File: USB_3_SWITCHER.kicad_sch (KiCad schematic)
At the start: 0 parts

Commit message: Arbeit
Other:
- sheet UPSTREAM_CON ports: added USB_UP_D_N, USB_UP_D_P, USB_UP_PORT_POWER_ON, USB_UP_SSRX_C_N, USB_UP_SSRX_C_P, USB_UP_SSTX_C_N, USB_UP_SSTX_C_P; removed none
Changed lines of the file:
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@@
 	)
 	(sheet
-		(at 135.89 133.35)
+		(at 134.62 133.35)
 		(size 41.91 59.69)
 		(exclude_from_sim no)
@@
 		)
 		(property "Sheetname" "HS_MUX"
-			(at 135.89 132.6384 0)
+			(at 134.62 132.6384 0)
 			(effects
 				(font
@@
 		)
 		(property "Sheetfile" "HS_MUX.kicad_sch"
-			(at 135.89 193.6246 0)
+			(at 134.62 193.6246 0)
 			(effects
 				(font
@@
 	(sheet
 		(at 320.04 99.06)
-		(size 30.48 25.4)
+		(size 30.48 30.48)
 		(exclude_from_sim no)
 		(in_bom yes)
@@
 		)
 		(property "Sheetfile" "DOWNSTREAM_CONNECOTRS.kicad_sch"
-			(at 320.04 125.0446 0)
+			(at 320.04 130.1246 0)
 			(effects
 				(font
@@
 	)
 	(sheet
-		(at 68.58 133.35)
-		(size 34.29 25.4)
+		(at 68.58 129.54)
+		(size 34.29 29.21)
 		(exclude_from_sim no)
 		(in_bom yes)
@@
 		)
 		(property "Sheetname" "UPSTREAM_CON"
-			(at 68.58 132.6384 0)
+			(at 68.58 128.8284 0)
 			(effects
 				(font
@@
 			)
 		)
+		(pin "USB_UP_D_P" bidirectional
+			(at 102.87 135.89 0)
+			(effects
+				(font
+					(size 1.27 1.27)
+				)
+				(justify right)
+			)
+		)
+		(pin "USB_UP_SSTX_C_N" input
+			(at 102.87 144.78 0)
+			(effects
+				(font
+					(size 1.27 1.27)
+				)
+				(justify right)
+			)
+		)
+		(pin "USB_UP_SSRX_C_P" output
+			(at 102.87 148.59 0)
+			(effects
+				(font
+					(size 1.27 1.27)
+				)
+				(justify right)
+			)
+		)
+		(pin "USB_UP_SSTX_C_P" input
+			(at 102.87 142.24 0)
+			(effects
+				(font
+					(size 1.27 1.27)
+				)
+				(justify right)
+			)
+		)
+		(pin "USB_UP_SSRX_C_N" output
+			(at 102.87 151.13 0)
+			(effects
+				(font
+					(size 1.27 1.27)
+				)
+				(justify right)
+			)
+		)
+		(pin "USB_UP_D_N" bidirectional
+			(at 102.87 138.43 0)
+			(effects
+				(font
+					(size 1.27 1.27)
+				)
+				(justify right)
+			)
+		)
+		(pin "USB_UP_PORT_POWER_ON" output
+			(at 102.87 154.94 0)
+			(effects
+				(font
+					(size 1.27 1.27)
+				)
+				(justify right)
+			)
+		)

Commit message: Weiter gearbeitet
Fast fertig:
HUB
Fertig
Connector (Up and Down)
MUX
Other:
- added sheet DIRECTION_SWITCH (DIRECTION_SWITCH.kicad_sch)
- added sheet DOWNSTREAM_CONNECTORS1 (DOWNSTREAM_CONNECOTRS.kicad_sch)
- added sheet DOWNSTREAM_CONNECTORS2 (DOWNSTREAM_CONNECOTRS.kicad_sch)
- added sheet DOWNSTREAM_CONNECTORS3 (DOWNSTREAM_CONNECOTRS.kicad_sch)
- added sheet EXTENSION_HEADER_DEBUG (EXTENSION_HEADER_DEBUG.kicad_sch)
- added sheet UPSTREAM_CON1 (UPSTREAM_CON.kicad_sch)
- sheet DOWNSTREAM_CONNECTORS ports: added USB_DS_D_N, USB_DS_D_P, USB_DS_SSRX_C_N, USB_DS_SSRX_C_P, USB_DS_SSTX_C_N, USB_DS_SSTX_C_P, VBUS_OUT_ON, ~{USB_DS_OC}; removed none
- sheet HS_MUX ports: added DIRECTION_SELECT, USB_UP1_D_N, USB_UP1_D_P, USB_UP1_SSRX_C_N, USB_UP1_SSRX_C_P, USB_UP1_SSTX_C_N, USB_UP1_SSTX_C_P, USB_UP2_D_N, USB_UP2_D_P, USB_UP2_SSRX_C_N, USB_UP2_SSRX_C_P, USB_UP2_SSTX_C_N, USB_UP2_SSTX_C_P, USB_UPSW_D_N, USB_UPSW_D_P, USB_UPSW_SSRX_C_N, USB_UPSW_SSRX_C_P, USB_UPSW_SSTX_C_N, USB_UPSW_SSTX_C_P, ~{MUX_OE}; removed none
- sheet USB_HUB ports: added SMB_SCL, SMB_SDA, USB_DS1_D_N, USB_DS1_D_P, USB_DS1_SSRX_C_N, USB_DS1_SSRX_C_P, USB_DS1_SSTX_C_N, USB_DS1_SSTX_C_P, USB_DS2_D_N, USB_DS2_D_P, USB_DS2_SSRX_C_N, USB_DS2_SSRX_C_P, USB_DS2_SSTX_C_N, USB_DS2_SSTX_C_P, USB_DS3_D_N, USB_DS3_D_P, USB_DS3_SSRX_C_N, USB_DS3_SSRX_C_P, USB_DS3_SSTX_C_N, USB_DS3_SSTX_C_P, USB_DS4_D_N, USB_DS4_D_P, USB_DS4_SSRX_C_N, USB_DS4_SSRX_C_P, USB_DS4_SSTX_C_N, USB_DS4_SSTX_C_P, USB_UPSW_D_N, USB_UPSW_D_P, USB_UPSW_SSRX_C_N, USB_UPSW_SSRX_C_P, USB_UPSW_SSTX_C_N, USB_UPSW_SSTX_C_P, VBUS_OUT1_ON, VBUS_OUT2_ON, VBUS_OUT3_ON, VBUS_OUT4_ON, ~{RESET}, ~{USB_DS1_OC}, ~{USB_DS2_OC}, ~{USB_DS3_OC}, ~{USB_DS4_OC}; removed none

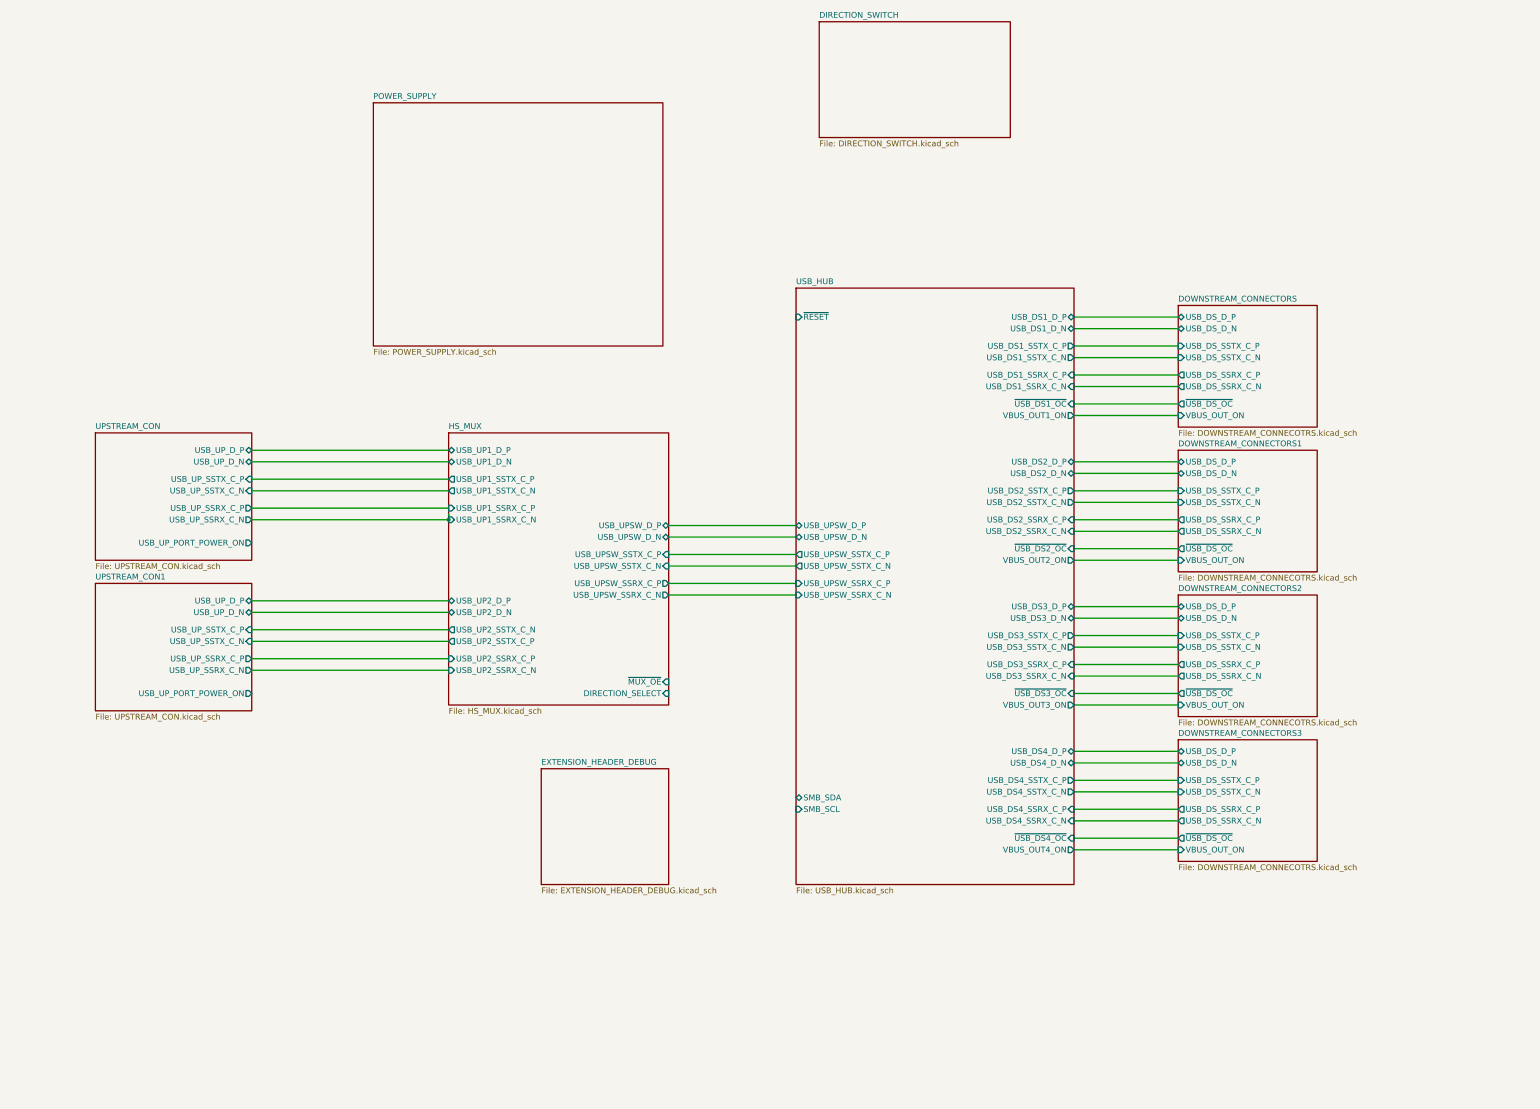
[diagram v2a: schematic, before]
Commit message: USB 3 Stecker ausgetauscht
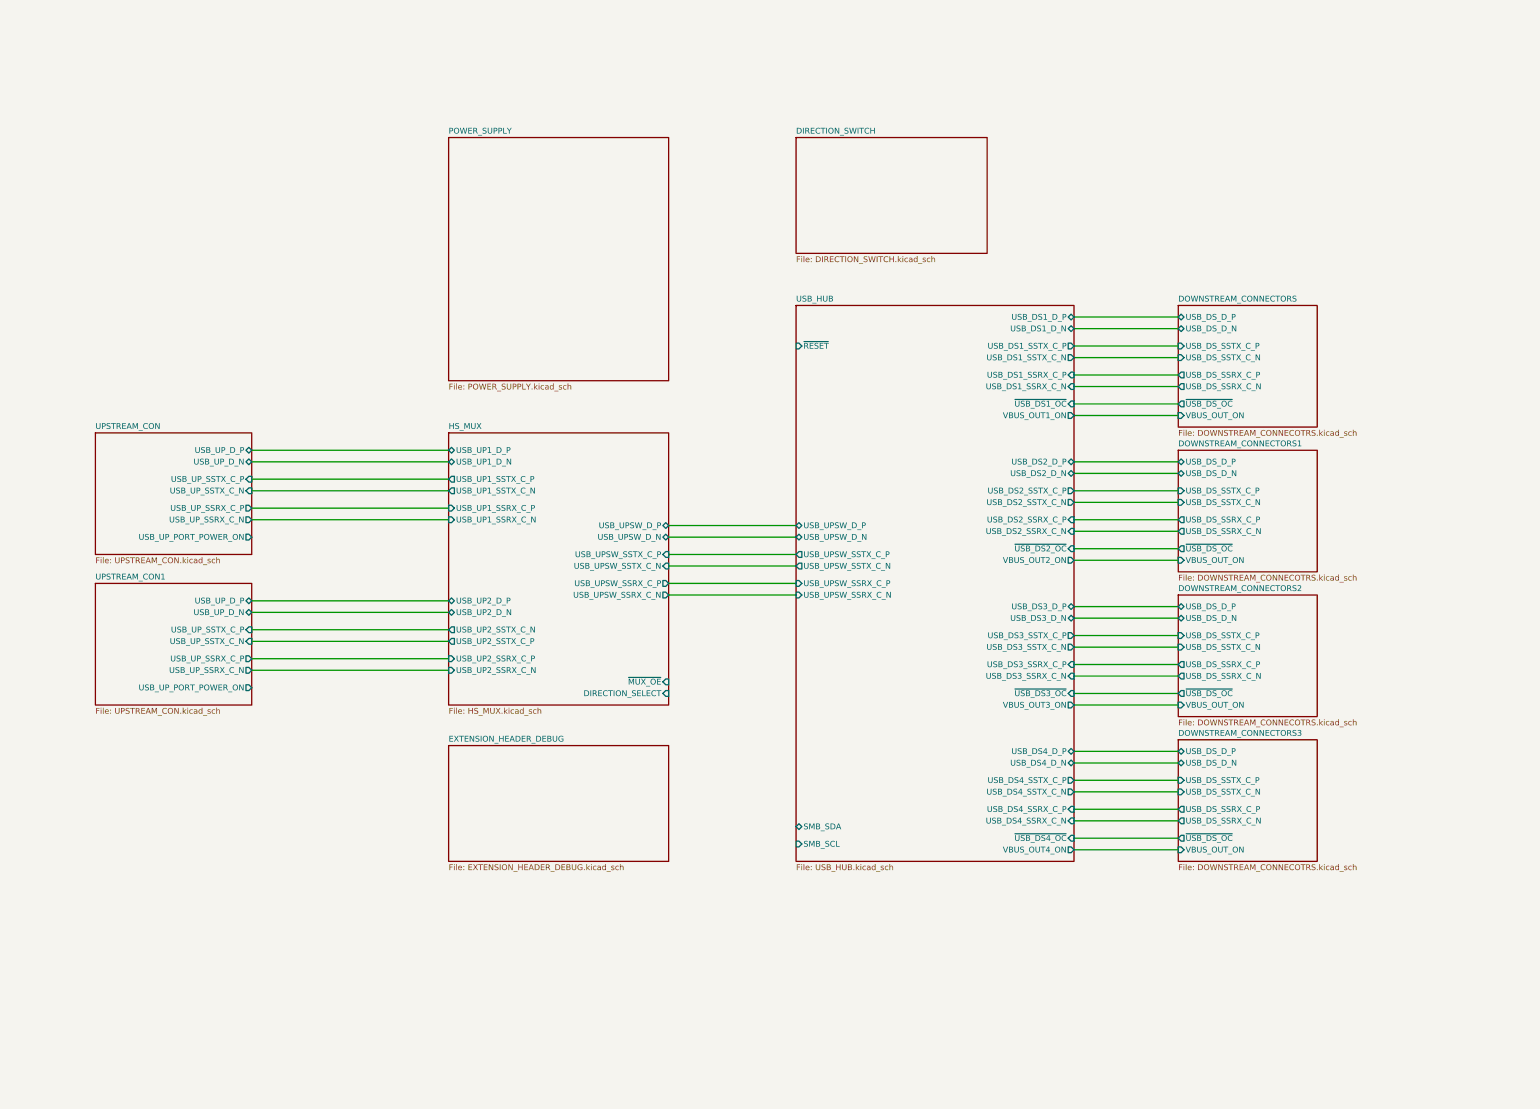
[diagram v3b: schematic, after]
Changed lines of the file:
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@@
 		(rev "Rev 1")
 	)
-	(junction
-		(at 130.81 152.4)
-		(diameter 0)
-		(color 0 0 0 0)
-	)
 	(wire
 		(pts
@@
 	(wire
 		(pts
-			(xy 130.81 152.4) (xy 130.81 151.13)
-		)
-		(stroke
-			(width 0)
-			(type default)
-		)
-	)
-	(wire
-		(pts
 			(xy 267.97 139.7) (xy 290.83 139.7)
 		)
@@
 	)
 	(sheet
-		(at 207.01 101.6)
-		(size 60.96 130.81)
+		(at 207.01 105.41)
+		(size 60.96 121.92)
 		(exclude_from_sim no)
 		(in_bom yes)
@@
 		)
 		(property "Sheetname" "USB_HUB"
-			(at 207.01 100.8884 0)
+			(at 207.01 104.6984 0)
 			(effects
 				(font
@@
 		)
 		(property "Sheetfile" "USB_HUB.kicad_sch"
-			(at 207.01 232.9946 0)
+			(at 207.01 227.9146 0)
 			(effects
 				(font
@@
 		)
 		(pin "SMB_SDA" bidirectional
-			(at 207.01 213.36 180)
+			(at 207.01 219.71 180)
 			(effects
 				(font
@@
 		)
 		(pin "~{RESET}" input
-			(at 207.01 107.95 180)
+			(at 207.01 114.3 180)
 			(effects
 				(font
@@
 		)
 		(pin "SMB_SCL" input
-			(at 207.01 215.9 180)
+			(at 207.01 223.52 180)
 			(effects
 				(font
@@
 	)
 	(sheet
-		(at 151.13 207.01)
-		(size 27.94 25.4)
+		(at 130.81 201.93)
+		(size 48.26 25.4)
 		(exclude_from_sim no)
 		(in_bom yes)
@@
 		)
 		(property "Sheetname" "EXTENSION_HEADER_DEBUG"
-			(at 151.13 206.2984 0)
+			(at 130.81 201.2184 0)
 			(effects
 				(font
@@
 		)
 		(property "Sheetfile" "EXTENSION_HEADER_DEBUG.kicad_sch"
-			(at 151.13 232.9946 0)
+			(at 130.81 227.9146 0)
 			(effects
 				(font
@@
 	(sheet
 		(at 53.34 133.35)
-		(size 34.29 27.94)
+		(size 34.29 26.67)
 		(exclude_from_sim no)
 		(in_bom yes)
@@
 		)
 		(property "Sheetfile" "UPSTREAM_CON.kicad_sch"
-			(at 53.34 161.8746 0)
+			(at 53.34 160.6046 0)
 			(effects
 				(font
@@
 		)
 		(pin "USB_UP_PORT_POWER_ON" output
-			(at 87.63 157.48 0)
+			(at 87.63 156.21 0)
 			(effects
 				(font
@@
 	)
 	(sheet
-		(at 114.3 60.96)
-		(size 63.5 53.34)
+		(at 130.81 68.58)
+		(size 48.26 53.34)
 		(exclude_from_sim no)
 		(in_bom yes)
@@
 		)
 		(property "Sheetname" "POWER_SUPPLY"
-			(at 114.3 60.2484 0)
+			(at 130.81 67.8684 0)
 			(effects
 				(font
@@
 		)
 		(property "Sheetfile" "POWER_SUPPLY.kicad_sch"
-			(at 114.3 114.8846 0)
+			(at 130.81 122.5046 0)
 			(effects
 				(font
@@
 	)
 	(sheet
-		(at 212.09 43.18)
+		(at 207.01 68.58)
 		(size 41.91 25.4)
 		(exclude_from_sim no)
@@
 		)
 		(property "Sheetname" "DIRECTION_SWITCH"
-			(at 212.09 42.4684 0)
+			(at 207.01 67.8684 0)
 			(effects
 				(font
@@
 		)
 		(property "Sheetfile" "DIRECTION_SWITCH.kicad_sch"
-			(at 212.09 69.1646 0)
+			(at 207.01 94.5646 0)
 			(effects
 				(font
@@
 	(sheet
 		(at 53.34 166.37)
-		(size 34.29 27.94)
+		(size 34.29 26.67)
 		(exclude_from_sim no)
 		(in_bom yes)
@@
 		)
 		(property "Sheetfile" "UPSTREAM_CON.kicad_sch"
-			(at 53.34 194.8946 0)
+			(at 53.34 193.6246 0)
 			(effects
 				(font
@@
 		)
 		(pin "USB_UP_PORT_POWER_ON" output
-			(at 87.63 190.5 0)
-			(effects
-				(font
+			(at 87.63 189.23 0)
+			(effects
+				(font

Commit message: Weiter gemacht
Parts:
- added H1, H2, H3, H4: MountingHole_Pad_MP, MountingHole:MountingHole_3.2mm_M3_DIN965_Pad_TopBottom, symbol Mechanical:MountingHole_Pad_MP
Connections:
- new net GND: H1.MP, H2.MP, H3.MP, H4.MP

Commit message: weiter gemacht
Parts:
- H2: footprint MountingHole:MountingHole_3.2mm_M3_DIN965_Pad_TopBottom -> MountingHole:MountingHole_3.2mm_M3_Pad_TopBottom

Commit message: Weiter gemacht
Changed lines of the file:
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@@
+	(wire
+		(pts
+			(xy 267.97 161.29) (xy 290.83 161.29)
+		)
+		(stroke
+			(width 0)
+			(type default)
+		)
+	)
+	(wire
+		(pts
+			(xy 87.63 182.88) (xy 130.81 182.88)
+		)
+		(stroke
+			(width 0)
+			(type default)
+		)
+	)
+	(wire
+		(pts
+			(xy 87.63 170.18) (xy 130.81 170.18)
+		)
+		(stroke
+			(width 0)
+			(type default)
+		)
+	)
+	(wire
+		(pts
+			(xy 267.97 107.95) (xy 290.83 107.95)
+		)
+		(stroke
+			(width 0)
+			(type default)
+		)
+	)
+	(wire
+		(pts
+			(xy 179.07 153.67) (xy 207.01 153.67)
+		)
+		(stroke
+			(width 0)
+			(type default)
+		)
+	)
+	(wire
+		(pts
+			(xy 179.07 168.91) (xy 207.01 168.91)
+		)
+		(stroke
+			(width 0)
+			(type default)
+		)
+	)
+	(wire
+		(pts
+			(xy 267.97 173.99) (xy 290.83 173.99)
+		)
+		(stroke
+			(width 0)
+			(type default)
+		)
+	)
+	(wire
+		(pts
+			(xy 87.63 146.05) (xy 130.81 146.05)
+		)
+		(stroke
+			(width 0)
+			(type default)
+		)
+	)
 	(wire
 		(pts
@@
 	(wire
 		(pts
-			(xy 267.97 161.29) (xy 290.83 161.29)
-		)
-		(stroke
-			(width 0)
-			(type default)
-		)
-	)
-	(wire
-		(pts
-			(xy 87.63 182.88) (xy 130.81 182.88)
-		)
-		(stroke
-			(width 0)
-			(type default)
-		)
-	)
-	(wire
-		(pts
-			(xy 87.63 170.18) (xy 130.81 170.18)
-		)
-		(stroke
-			(width 0)
-			(type default)
-		)
-	)
-	(wire
-		(pts
-			(xy 267.97 107.95) (xy 290.83 107.95)
-		)
-		(stroke
-			(width 0)
-			(type default)
-		)
-	)
-	(wire
-		(pts
-			(xy 179.07 153.67) (xy 207.01 153.67)
-		)
-		(stroke
-			(width 0)
-			(type default)
-		)
-	)
-	(wire
-		(pts
-			(xy 179.07 168.91) (xy 207.01 168.91)
-		)
-		(stroke
-			(width 0)
-			(type default)
-		)
-	)
-	(wire
-		(pts
-			(xy 267.97 173.99) (xy 290.83 173.99)
-		)
-		(stroke
-			(width 0)
-			(type default)
-		)
-	)
-	(wire
-		(pts
-			(xy 87.63 146.05) (xy 130.81 146.05)
-		)
-		(stroke
-			(width 0)
-			(type default)
-		)
-	)
-	(wire
-		(pts
 			(xy 267.97 205.74) (xy 290.83 205.74)
 		)
@@
 	(wire
 		(pts
+			(xy 87.63 176.53) (xy 130.81 176.53)
+		)
+		(stroke
+			(width 0)
+			(type default)
+		)
+	)
+	(wire
+		(pts
 			(xy 87.63 172.72) (xy 130.81 172.72)
 		)
@@
 		(pts
 			(xy 36.83 274.32) (xy 36.83 273.05)
-		)
-		(stroke
-			(width 0)
-			(type default)
-		)
-	)
-	(wire
-		(pts
-			(xy 87.63 176.53) (xy 130.81 176.53)
 		)
 		(stroke
@@
 		)
 		(pin "USB_UP2_SSTX_C_N" output
+			(at 130.81 179.07 180)
+			(effects
+				(font
+					(size 1.27 1.27)
+				)
+				(justify left)
+			)
+		)
+		(pin "USB_UP2_SSTX_C_P" output
 			(at 130.81 176.53 180)
 			(effects
 				(font
-					(size 1.27 1.27)
-				)
-				(justify left)
-			)
-		)
-		(pin "USB_UP2_SSTX_C_P" output
-			(at 130.81 179.07 180)
-			(effects
-				(font

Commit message: Layout + Schematic weiter gemacht
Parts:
- removed H1, H3, H4: MountingHole_Pad_MP, MountingHole:MountingHole_3.2mm_M3_DIN965_Pad_TopBottom, symbol Mechanical:MountingHole_Pad_MP
- removed H2: MountingHole_Pad_MP, MountingHole:MountingHole_3.2mm_M3_Pad_TopBottom, symbol Mechanical:MountingHole_Pad_MP

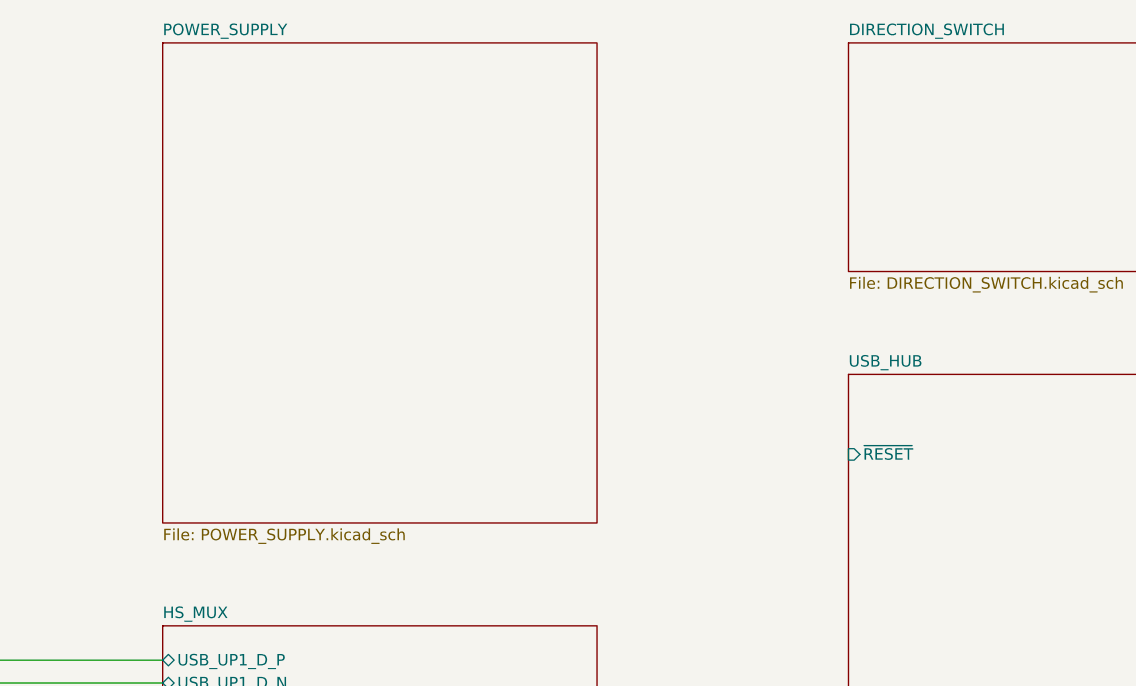
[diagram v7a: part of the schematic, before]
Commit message: Button & Power Sequencing + Layout
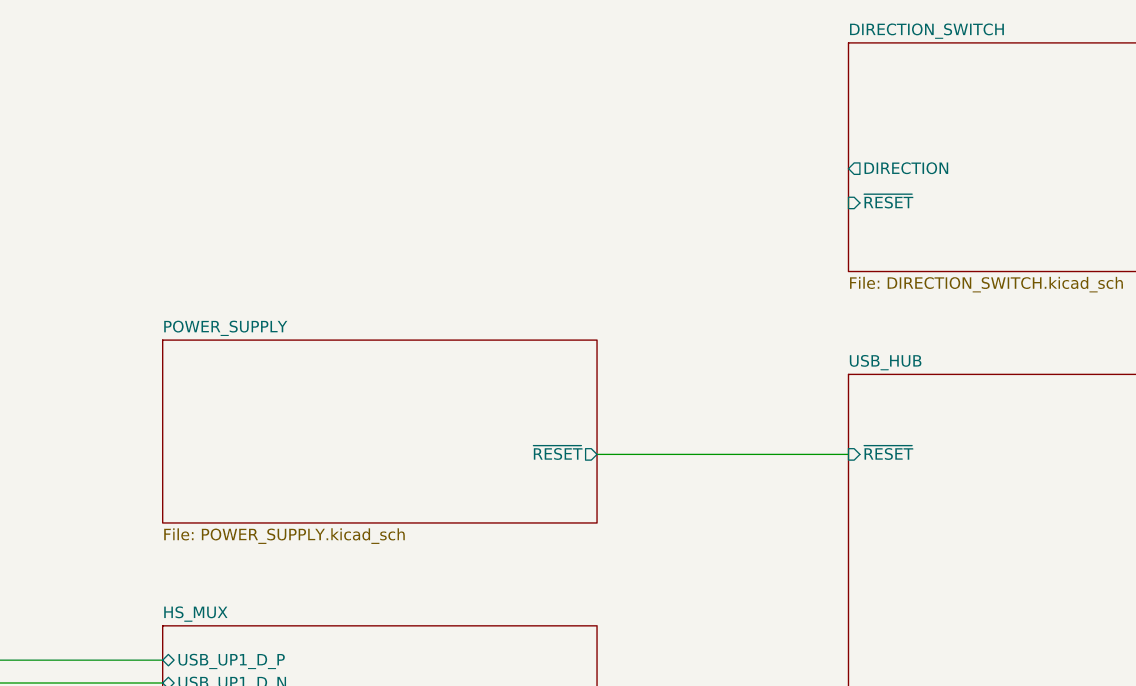
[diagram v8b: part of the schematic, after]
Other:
- sheet DIRECTION_SWITCH ports: added DIRECTION, ~{RESET}; removed none
- sheet POWER_SUPPLY ports: added ~{RESET}; removed none
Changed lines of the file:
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@@
+	(wire
+		(pts
+			(xy 179.07 114.3) (xy 207.01 114.3)
+		)
+		(stroke
+			(width 0)
+			(type default)
+		)
+	)
 	(wire
 		(pts
@@
 	)
 	(sheet
-		(at 130.81 68.58)
-		(size 48.26 53.34)
+		(at 130.81 101.6)
+		(size 48.26 20.32)
 		(exclude_from_sim no)
 		(in_bom yes)
@@
 		)
 		(property "Sheetname" "POWER_SUPPLY"
-			(at 130.81 67.8684 0)
+			(at 130.81 100.8884 0)
 			(show_name no)
 			(do_not_autoplace no)
@@
 				)
 				(justify left top)
+			)
+		)
+		(pin "~{RESET}" output
+			(at 179.07 114.3 0)
+			(effects
+				(font
+					(size 1.27 1.27)
+				)
+				(justify right)
 			)
 		)
@@
 			)
 		)
+		(pin "DIRECTION" output
+			(at 207.01 82.55 180)
+			(effects
+				(font
+					(size 1.27 1.27)
+				)
+				(justify left)
+			)
+		)
+		(pin "~{RESET}" input
+			(at 207.01 86.36 180)
+			(effects
+				(font
+					(size 1.27 1.27)
+				)
+				(justify left)
+			)
+		)
